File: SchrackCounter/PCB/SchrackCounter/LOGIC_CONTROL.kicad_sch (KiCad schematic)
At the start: 2 parts, among them U1 74HC595

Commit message: update
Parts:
- removed AFF1: LTS-6960HR, Display_7Segment:7SegmentLED_LTS6760_LTS6780, symbol Display_Character:LTS-6960HR
- removed U1: 74HC595, symbol 74xx:74HC595
- added U?: MAX7221xWG, Package_SO:SOIC-24W_7.5x15.4mm_P1.27mm, symbol Driver_LED:MAX7221xWG
- added U?: DC56-11EWA, Display_7Segment:DA56-11SURKWA, symbol Display_Character:DC56-11EWA
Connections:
- new net: U?.4 (GND), U?.9 (GND)
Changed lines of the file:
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@@
 	)
 	(symbol
-		(lib_id "Display_Character:LTS-6960HR")
-		(at 121.92 62.23 0)
+		(lib_id "Driver_LED:MAX7221xWG")
+		(at 36.83 50.8 0)
+		(unit 1)
+		(exclude_from_sim no)
+		(in_bom yes)
+		(on_board yes)
+		(dnp no)
+		(property "Reference" "U?"
+			(at 39.0541 22.86 0)
+			(effects
+				(font
+					(size 1.27 1.27)
+				)
+				(justify left)
+			)
+		)
+		(property "Value" "MAX7221xWG"
+			(at 39.0541 25.4 0)
+			(effects
+				(font
+					(size 1.27 1.27)
+				)
+				(justify left)
+			)
+		)
+		(property "Footprint" "Package_SO:SOIC-24W_7.5x15.4mm_P1.27mm"
+			(at 35.56 49.53 0)
+			(effects
+				(font
+					(size 1.27 1.27)
+				)
+				(hide yes)
+			)
+		)
+		(property "Datasheet" "https://datasheets.maximintegrated.com/en/ds/MAX7219-MAX7221.pdf"
+			(at 38.1 54.61 0)
+			(effects
+				(font
+					(size 1.27 1.27)
+				)
+				(hide yes)
+			)
+		)
+		(property "Description" "Serially Interfaced, 8-Digit LED Display Driver, SOIC-24W"
+			(at 36.83 50.8 0)
+			(effects
+				(font
+					(size 1.27 1.27)
+				)
+				(hide yes)
+			)
+		)
+		(pin "12"
+		)
+		(pin "16"
+		)
+		(pin "9"
+		)
+		(pin "13"
+		)
+		(pin "17"
+		)
+		(pin "23"
+		)
+		(pin "4"
+		)
+		(pin "2"
+		)
+		(pin "24"
+		)
+		(pin "5"
+		)
+		(pin "11"
+		)
+		(pin "18"
+		)
+		(pin "7"
+		)
+		(pin "6"
+		)
+		(pin "1"
+		)
+		(pin "10"
+		)
+		(pin "20"
+		)
+		(pin "21"
+		)
+		(pin "3"
+		)
+		(pin "14"
+		)
+		(pin "8"
+		)
+		(pin "19"
+		)
+		(pin "22"
+		)
+		(pin "15"
+		)
+		(instances
+			(project ""
+				(path "/d96f2ffc-3f4c-4f71-b693-29f6b8c3245d/50491303-1200-42ed-9e6c-90c20c198c18"
+					(reference "U?")
+					(unit 1)
+				)
+			)
+		)
+	)
+	(symbol
+		(lib_id "Display_Character:DC56-11EWA")
+		(at 109.22 48.26 0)
 		(unit 1)
 		(exclude_from_sim no)
@@
 		(dnp no)
 		(fields_autoplaced yes)
-		(property "Reference" "AFF1"
-			(at 121.92 44.45 0)
-			(effects
-				(font
-					(size 1.27 1.27)
-				)
-			)
-		)
-		(property "Value" "LTS-6960HR"
-			(at 121.92 46.99 0)
-			(effects
-				(font
-					(size 1.27 1.27)
-				)
-			)
-		)
-		(property "Footprint" "Display_7Segment:7SegmentLED_LTS6760_LTS6780"
-			(at 121.92 77.47 0)
-			(effects
-				(font
-					(size 1.27 1.27)
-				)
-				(hide yes)
-			)
-		)
-		(property "Datasheet" "https://datasheet.octopart.com/LTS-6960HR-Lite-On-datasheet-11803242.pdf"
-			(at 121.92 62.23 0)
-			(effects
-				(font
-					(size 1.27 1.27)
-				)
-				(hide yes)
-			)
-		)
-		(property "Description" "DISPLAY 7 SEGMENTS common A."
-			(at 121.92 62.23 0)
-			(effects
-				(font
-					(size 1.27 1.27)
-				)
-				(hide yes)
-			)
+		(property "Reference" "U?"
+			(at 109.22 30.48 0)
+			(effects
+				(font
+					(size 1.27 1.27)
+				)
+			)
+		)
+		(property "Value" "DC56-11EWA"
+			(at 109.22 33.02 0)
+			(effects
+				(font
+					(size 1.27 1.27)
+				)
+			)
+		)
+		(property "Footprint" "Display_7Segment:DA56-11SURKWA"
+			(at 109.728 64.77 0)
+			(effects
+				(font
+					(size 1.27 1.27)
+				)
+				(hide yes)
+			)
+		)
+		(property "Datasheet" "http://www.kingbrightusa.com/images/catalog/SPEC/DC56-11EWA.pdf"
+			(at 106.172 45.72 0)
+			(effects
+				(font
+					(size 1.27 1.27)
+				)
+				(hide yes)
+			)
+		)
+		(property "Description" "Double digit 7 segment super bright red LED common cathode"
+			(at 109.22 48.26 0)
+			(effects
+				(font
+					(size 1.27 1.27)
+				)
+				(hide yes)
+			)
+		)
+		(pin "5"
 		)
 		(pin "7"
@@
 		(pin "4"
 		)
+		(pin "15"
+		)
+		(pin "11"
+		)
+		(pin "9"
+		)
+		(pin "16"
+		)
+		(pin "6"
+		)
+		(pin "14"
+		)
+		(pin "1"
+		)
+		(pin "17"
+		)
 		(pin "8"
 		)
+		(pin "10"
+		)
 		(pin "2"
 		)
-		(pin "6"
+		(pin "18"
+		)
+		(pin "12"
 		)
 		(pin "3"
 		)
-		(pin "9"
-		)
-		(pin "1"
-		)
-		(pin "10"
-		)
-		(pin "5"
+		(pin "13"
 		)
 		(instances
 			(project ""
 				(path "/d96f2ffc-3f4c-4f71-b693-29f6b8c3245d/50491303-1200-42ed-9e6c-90c20c198c18"
-					(reference "AFF1")
+					(reference "U?")
 					(unit 1)
 				)
-			)
-		)
-	)
-	(symbol
-		(lib_id "74xx:74HC595")
-		(at 156.21 59.69 0)
-		(unit 1)
-		(exclude_from_sim no)
-		(in_bom yes)
-		(on_board yes)
-		(dnp no)
-		(fields_autoplaced yes)
-		(property "Reference" "U1"
-			(at 158.4341 41.91 0)
-			(effects
-				(font
-					(size 1.27 1.27)
-				)
-				(justify left)
-			)
-		)
-		(property "Value" "74HC595"
-			(at 158.4341 44.45 0)
-			(effects
-				(font
-					(size 1.27 1.27)
-				)
-				(justify left)
-			)
-		)
-		(property "Footprint" ""
-			(at 156.21 59.69 0)
-			(effects
-				(font
-					(size 1.27 1.27)
-				)
-				(hide yes)
-			)
-		)
-		(property "Datasheet" "http://www.ti.com/lit/ds/symlink/sn74hc595.pdf"
-			(at 156.21 59.69 0)
-			(effects
-				(font
-					(size 1.27 1.27)
-				)
-				(hide yes)
-			)
-		)
-		(property "Description" "8-bit serial in/out Shift Register 3-State Outputs"
-			(at 156.21 59.69 0)
-			(effects
-				(font
-					(size 1.27 1.27)
-				)
-				(hide yes)
-			)
-		)
-		(pin "2"
-		)
-		(pin "12"
-		)
-		(pin "15"
-		)
-		(pin "6"
-		)
-		(pin "16"
-		)
-		(pin "11"
-		)
-		(pin "10"
-		)
-		(pin "9"
-		)
-		(pin "8"
-		)
-		(pin "4"
-		)
-		(pin "3"
-		)
-		(pin "7"
-		)
-		(pin "14"
-		)
-		(pin "1"
-		)
-		(pin "5"
-		)
-		(pin "13"
-		)
-		(instances
-			(project ""
-				(path "/d96f2ffc-3f4c-4f71-b693-29f6b8c3245d/50491303-1200-42ed-9e6c-90c20c198c18"
-					(reference "U1")
-					(unit 1)
-				)

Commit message: Schematic update
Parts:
- removed U?: MAX7221xWG, Package_SO:SOIC-24W_7.5x15.4mm_P1.27mm, symbol Driver_LED:MAX7221xWG
- added C10: 100nF.mcu, Capacitor_SMD:C_0805_2012Metric_Pad1.18x1.45mm_HandSolder, symbol Device:C
- added C9: 10uF.mcu, Capacitor_Tantalum_SMD:CP_EIA-3216-18_Kemet-A_Pad1.58x1.35mm_HandSolder, symbol Device:C_Polarized
- added R3: 10k, symbol Device:R
- added U1, U3, U5: D168K, Display_7Segment:D1X8K, symbol Display_Character:D168K
- added U2: DC56-11EWA, Display_7Segment:DA56-11SURKWA, symbol Display_Character:DC56-11EWA
- added U6: MAX7219, symbol Driver_LED:MAX7219
- gave numbers to parts that had none: 1
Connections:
- net SEG_E: now reaches U4.1 (DIG1_E)
- net SEG_E: now also U4.5 (DIG2_E), U1.1 (E), U2.1 (DIG1_E), U2.5 (DIG2_E), U3.1 (E), U5.1 (E), U6.21 (SEG_E)
- net SEG_B: now reaches U4.10 (DIG2_B)
- net SEG_B: now also U4.15 (DIG1_B), U1.6 (B), U2.10 (DIG2_B), U2.15 (DIG1_B), U3.6 (B), U5.6 (B), U6.16 (SEG_B)
- net SEG_A: now reaches U4.11 (DIG2_A)
- net SEG_A: now also U4.16 (DIG1_A), U1.7 (A), U2.11 (DIG2_A), U2.16 (DIG1_A), U3.7 (A), U5.7 (A), U6.14 (SEG_A)
- net SEG_F: now reaches U4.12 (DIG2_F)
- net SEG_F: now also U4.18 (DIG1_F), U1.9 (F), U2.12 (DIG2_F), U2.18 (DIG1_F), U3.9 (F), U5.9 (F), U6.15 (SEG_F)
- net GND: now reaches U4.13 (DIG2_CC)
- net GND: now also U4.14 (DIG1_CC), C10.2, C9.2, U1.3 (CC), U1.8 (CC), U2.13 (DIG2_CC), U2.14 (DIG1_CC), U3.3 (CC), U3.8 (CC), U5.3 (CC), U5.8 (CC), U6.4 (GND), U6.9 (GND)
- net SEG_G: now reaches U4.17 (DIG1_G)
- net SEG_G: now also U4.7 (DIG2_G), U1.10 (G), U2.17 (DIG1_G), U2.7 (DIG2_G), U3.10 (G), U5.10 (G), U6.17 (SEG_G)
- net SEG_D: now reaches U4.2 (DIG1_D)
- net SEG_D: now also U4.6 (DIG2_D), U1.2 (D), U2.2 (DIG1_D), U2.6 (DIG2_D), U3.2 (D), U5.2 (D), U6.23 (SEG_D)
- net SEG_C: now reaches U4.3 (DIG1_C)
- net SEG_C: now also U4.8 (DIG2_C), U1.4 (C), U2.3 (DIG1_C), U2.8 (DIG2_C), U3.4 (C), U5.4 (C), U6.20 (SEG_C)
- net DP0: now reaches U4.4 (DP1)
- net DP0: now also U6.2 (DIG_0)
- net DP1: now reaches U4.9 (DP2)
- net DP1: now also U6.11 (DIG_1)
- new net: R3.2, U6.18 (ISET)
- new net +5V: C10.1, C9.1, R3.1, U6.19 (V+)
- new net DP2: U2.9 (DP2), U6.6 (DIG_2)
- new net DP3: U2.4 (DP1), U6.7 (DIG_3)
- new net DP4: U1.5 (DP), U6.3 (DIG_4)
- new net DP5: U3.5 (DP), U6.10 (DIG_5)
- new net DP6: U5.5 (DP), U6.5 (DIG_6)
- new net MOSI: U6.1 (DIN)
- new net SCK: U6.13 (CLK)
- new net ~{CS}: U6.12 (LOAD)
- no-connect marks 0 -> 2
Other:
- note added: "DRIVERS"
- note added: "SCORE"
- note added: "TIME"
- moved on the sheet: U4

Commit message: Schematic update
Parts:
- C10: value 100nF.mcu -> 100nF.max
- C9: value 10uF.mcu -> 10uF.max
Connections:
- net SCK renamed CLK
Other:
- moved on the sheet: C10, C9, R3, U1, U2, U3, U4, U5, U6

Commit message: sleep, overated imo
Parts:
- R3: footprint (none) -> Resistor_SMD:R_0805_2012Metric_Pad1.20x1.40mm_HandSolder
- U6: footprint (none) -> Package_SO:SOIC-24W_7.5x15.4mm_P1.27mm
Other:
- moved on the sheet: C10, C9, R3, U1, U2, U3, U4, U5, U6

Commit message: pcb Update
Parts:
- added U9: CA56-12SURKWA, Display_7Segment:CA56-12SURKWA, symbol Display_Character:CA56-12SURKWA
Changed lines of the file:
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@@
+	)
+	(symbol
+		(lib_id "Display_Character:CA56-12SURKWA")
+		(at 6.35 57.15 0)
+		(unit 1)
+		(exclude_from_sim no)
+		(in_bom yes)
+		(on_board yes)
+		(dnp no)
+		(fields_autoplaced yes)
+		(property "Reference" "U9"
+			(at 6.35 39.37 0)
+			(effects
+				(font
+					(size 1.27 1.27)
+				)
+			)
+		)
+		(property "Value" "CA56-12SURKWA"
+			(at 6.35 41.91 0)
+			(effects
+				(font
+					(size 1.27 1.27)
+				)
+			)
+		)
+		(property "Footprint" "Display_7Segment:CA56-12SURKWA"
+			(at 6.35 72.39 0)
+			(effects
+				(font
+					(size 1.27 1.27)
+				)
+				(hide yes)
+			)
+		)
+		(property "Datasheet" "http://www.kingbright.com/attachments/file/psearch/000/00/00/CA56-12SURKWA(Ver.8A).pdf"
+			(at -4.572 56.388 0)
+			(effects
+				(font
+					(size 1.27 1.27)
+				)
+				(hide yes)
+			)
+		)
+		(property "Description" "4 digit 7 segment hyper red LED, common anode"
+			(at 6.35 57.15 0)
+			(effects
+				(font
+					(size 1.27 1.27)
+				)
+				(hide yes)
+			)
+		)
+		(pin "5"
+		)
+		(pin "9"
+		)
+		(pin "4"
+		)
+		(pin "10"
+		)
+		(pin "1"
+		)
+		(pin "2"
+		)
+		(pin "3"
+		)
+		(pin "11"
+		)
+		(pin "7"
+		)
+		(pin "12"
+		)
+		(pin "6"
+		)
+		(pin "8"
+		)
+		(instances
+			(project ""
+				(path "/d96f2ffc-3f4c-4f71-b693-29f6b8c3245d/50491303-1200-42ed-9e6c-90c20c198c18"
+					(reference "U9")
+					(unit 1)
+				)
+			)
+		)
 	)
 	(symbol

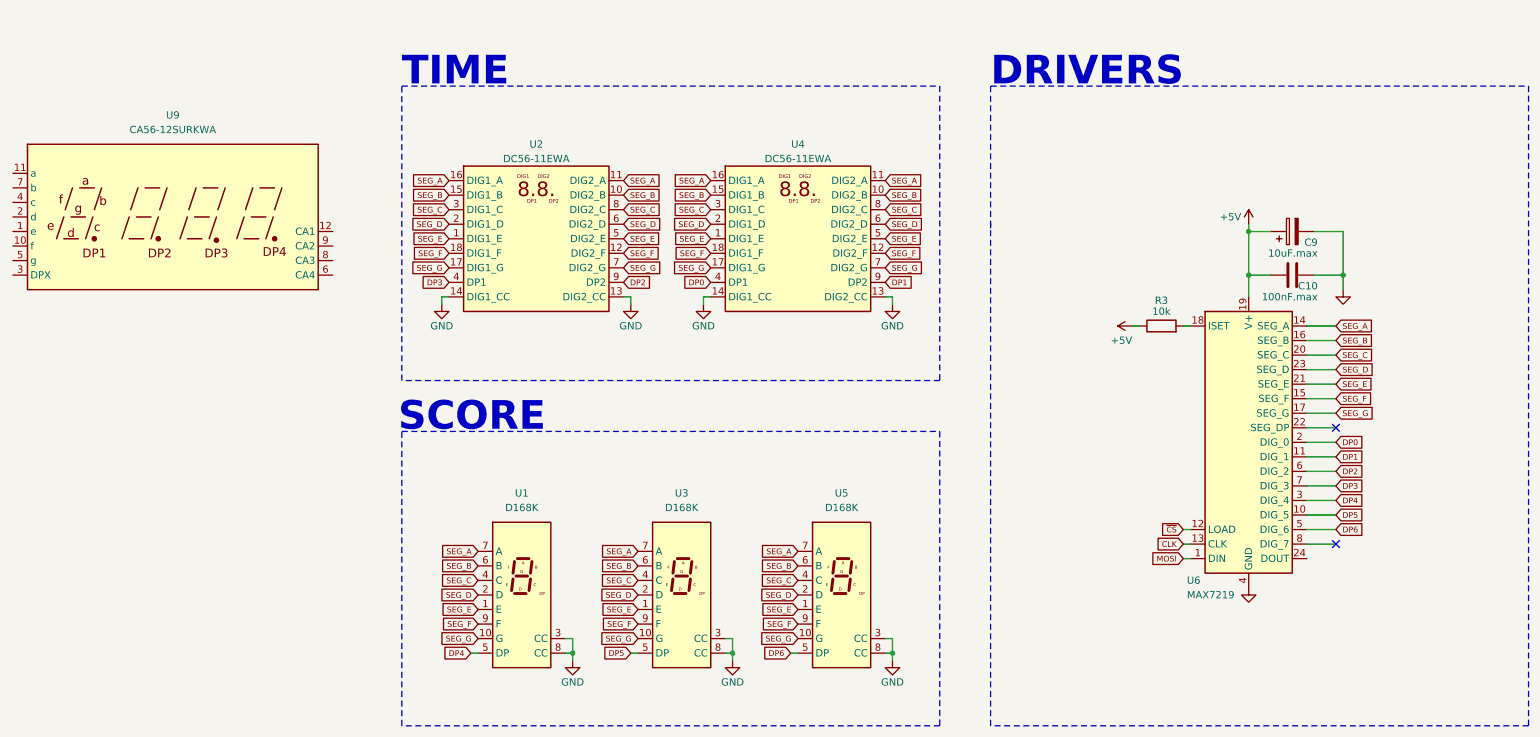
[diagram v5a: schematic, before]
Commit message: Custom symbol and footprints
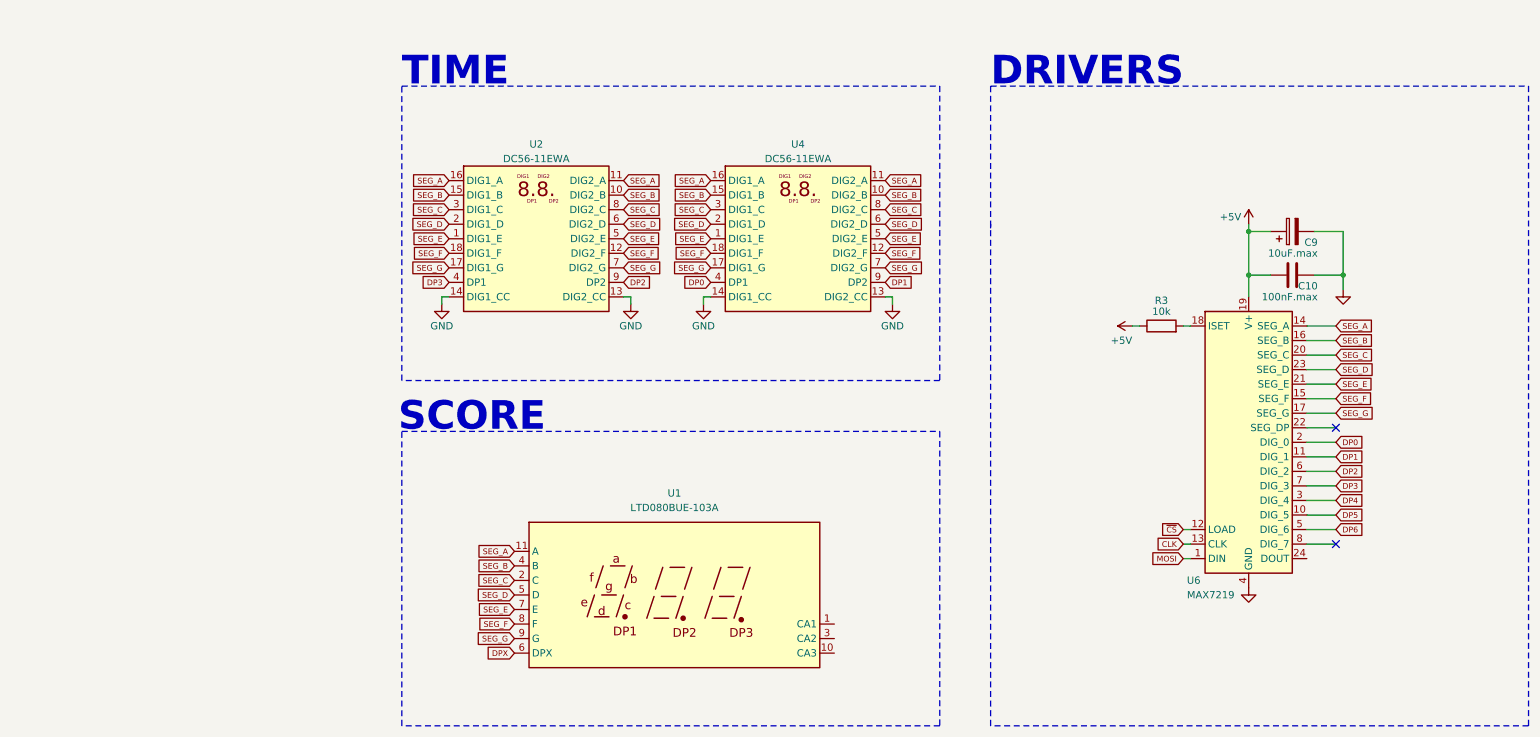
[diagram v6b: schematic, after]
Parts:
- removed U1, U3, U5: D168K, Display_7Segment:D1X8K, symbol Display_Character:D168K
- removed U9: CA56-12SURKWA, Display_7Segment:CA56-12SURKWA, symbol Display_Character:CA56-12SURKWA
- added U1: LTD080BUE-103A, Schrack_brd:LTD080BUE-103A made_by_bismarx, symbol sumec_sch_lib:LTD080BUE-103A_made_by_bismarx
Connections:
- net SEG_A: now also U1.11 (A)
- net SEG_B: now also U1.4 (B)
- net SEG_C: now also U1.2 (C)
- net SEG_D: now also U1.5 (D)
- net SEG_E: now also U1.7 (E)
- net SEG_F: now also U1.8 (F)
- net SEG_G: now also U1.9 (G)
- new net DPX: U1.6 (DPX)

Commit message: deletion of useless shit
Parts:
- U1: footprint Schrack_brd:LTD080BUE-103A made_by_bismarx -> Schrack_brd:LTD080BUE-103A_made_by_bismarx
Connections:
- net +3V3: now reaches U1.1 (CA1)
- net +3V3: now also U1.10 (CA3), U1.3 (CA2)
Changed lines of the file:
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@@
+	)
+	(junction
+		(at 124.46 128.27)
+		(diameter 0)
+		(color 0 0 0 0)
+	)
+	(junction
+		(at 124.46 130.81)
+		(diameter 0)
+		(color 0 0 0 0)
 	)
 	(junction
@@
 	(wire
 		(pts
+			(xy 125.73 128.27) (xy 124.46 128.27)
+		)
+		(stroke
+			(width 0)
+			(type default)
+		)
+	)
+	(wire
+		(pts
 			(xy 99.06 71.12) (xy 100.33 71.12)
 		)
@@
 	(wire
 		(pts
+			(xy 121.92 130.81) (xy 124.46 130.81)
+		)
+		(stroke
+			(width 0)
+			(type default)
+		)
+	)
+	(wire
+		(pts
 			(xy 205.74 67.31) (xy 210.82 67.31)
 		)
@@
 	(wire
 		(pts
+			(xy 124.46 130.81) (xy 124.46 128.27)
+		)
+		(stroke
+			(width 0)
+			(type default)
+		)
+	)
+	(wire
+		(pts
 			(xy 209.55 106.68) (xy 204.47 106.68)
 		)
@@
 	(wire
 		(pts
+			(xy 124.46 128.27) (xy 121.92 128.27)
+		)
+		(stroke
+			(width 0)
+			(type default)
+		)
+	)
+	(wire
+		(pts
 			(xy 99.06 71.12) (xy 99.06 72.39)
 		)
@@
 	(wire
 		(pts
+			(xy 121.92 133.35) (xy 124.46 133.35)
+		)
+		(stroke
+			(width 0)
+			(type default)
+		)
+	)
+	(wire
+		(pts
 			(xy 132.08 71.12) (xy 130.81 71.12)
 		)
@@
 		(pts
 			(xy 209.55 88.9) (xy 204.47 88.9)
+		)
+		(stroke
+			(width 0)
+			(type default)
+		)
+	)
+	(wire
+		(pts
+			(xy 124.46 133.35) (xy 124.46 130.81)
 		)
 		(stroke
@@
 			)
 		)
-		(property "Footprint" "Schrack_brd:LTD080BUE-103A made_by_bismarx"
+		(property "Footprint" "Schrack_brd:LTD080BUE-103A_made_by_bismarx"
 			(at 93.98 138.43 0)
 			(effects
@@
 					(unit 1)
 				)
+			)
+		)
+	)
+	(symbol
+		(lib_id "power:+3V3")
+		(at 125.73 128.27 270)
+		(unit 1)
+		(exclude_from_sim no)
+		(in_bom yes)
+		(on_board yes)
+		(dnp no)
+		(property "Reference" "#PWR013"
+			(at 121.92 128.27 0)
+			(effects
+				(font
+					(face "Bahnschrift")
+					(size 1.27 1.27)
+				)
+				(hide yes)
+			)
+		)
+		(property "Value" "+3V3"
+			(at 129.54 128.27 90)
+			(effects
+				(font
+					(face "Bahnschrift")
+					(size 1.27 1.27)
+				)
+				(justify left)
+			)
+		)
+		(property "Footprint" ""
+			(at 125.73 128.27 0)
+			(effects
+				(font
+					(face "Bahnschrift")
+					(size 1.27 1.27)
+				)
+				(hide yes)
+			)
+		)
+		(property "Datasheet" ""
+			(at 125.73 128.27 0)
+			(effects
+				(font
+					(face "Bahnschrift")
+					(size 1.27 1.27)
+				)
+				(hide yes)
+			)
+		)
+		(property "Description" ""
+			(at 125.73 128.27 0)
+			(effects
+				(font
+					(size 1.27 1.27)
+				)
+				(hide yes)
+			)
+		)
+		(pin "1"
+		)
+		(instances
+			(project "SchrackCounter"
+				(path "/d96f2ffc-3f4c-4f71-b693-29f6b8c3245d/50491303-1200-42ed-9e6c-90c20c198c18"
+					(reference "#PWR013")
+					(unit 1)
+				)
